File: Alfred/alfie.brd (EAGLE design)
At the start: 82.6 x 45 mm, 19 parts, among them IC1 7805TV, K1 G6A-234P, K2 G6A-234P

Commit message: Added diodes and resistors.
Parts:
- added D5, D6: 1N4148DO35-7, diode:DO35-7
- added R1: (no value), rcl:0207/10
- moved U$5 5.75 mm to (45.7, 10.2), turned to 90 degrees
- moved U$2 5.12 mm to (45.7, 21.6), turned to 90 degrees
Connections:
- net +5V: now also D5.C, D6.C
- net DOORBELL: now also R1.2
- net GND: now also R1.1
- net N$1: now also D6.A
- net N$2: now also D5.A
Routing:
- net +5V: track 166.1 -> 171.2 mm
- net N$2: track 5.60 -> 6.36 mm
- net N$1: track 5.86 -> 6.36 mm
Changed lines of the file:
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@@
 <element name="IC1" library="linear" package="TO220V" value="7805TV" x="53.34" y="38.1" rot="R90"/>
 <element name="C2" library="rcl" package="C025-030X050" value="" x="52.07" y="39.37" rot="R270"/>
-<element name="U$2" library="NTF3055L108" package="SOT223" value="NTF3055L108T1GTAB" x="46.355" y="26.67" rot="MR180"/>
+<element name="U$2" library="NTF3055L108" package="SOT223" value="NTF3055L108T1GTAB" x="45.72" y="21.59" rot="MR90"/>
 <element name="K1" library="relay" package="G6A-234P" value="G6A-234P" x="55.245" y="21.59">
 <attribute name="OC_NEWARK" value="unknown" x="55.245" y="21.59" size="1.778" layer="27" display="off"/>
@@
 <attribute name="OC_FARNELL" value="unknown" x="20.955" y="25.4" size="1.778" layer="27" rot="R270" display="off"/>
 </element>
-<element name="U$5" library="NTF3055L108" package="SOT223" value="NTF3055L108T1GTAB" x="46.355" y="15.875" rot="MR180"/>
+<element name="U$5" library="NTF3055L108" package="SOT223" value="NTF3055L108T1GTAB" x="45.72" y="10.16" rot="MR90"/>
 <element name="K2" library="relay" package="G6A-234P" value="G6A-234P" x="55.245" y="10.16">
 <attribute name="OC_NEWARK" value="unknown" x="46.355" y="10.16" size="1.778" layer="27" display="off"/>
@@
 <attribute name="OC_FARNELL" value="unknown" x="75.565" y="8.89" size="1.778" layer="27" rot="R90" display="off"/>
 </element>
+<element name="D5" library="diode" package="DO35-7" value="1N4148DO35-7" x="48.895" y="10.16" rot="R90"/>
+<element name="D6" library="diode" package="DO35-7" value="1N4148DO35-7" x="48.895" y="21.59" rot="R90"/>
+<element name="R1" library="rcl" package="0207/10" value="" x="39.37" y="35.56" rot="R90"/>
 </elements>
 <signals>
@@
 <wire x1="52.705" y1="17.78" x2="51.435" y2="17.78" width="0.8128" layer="16"/>
 <wire x1="51.435" y1="6.35" x2="53.975" y2="6.35" width="0.8128" layer="16"/>
+<contactref element="D5" pad="C"/>
+<contactref element="D6" pad="C"/>
+<wire x1="48.895" y1="6.35" x2="51.435" y2="6.35" width="0.8128" layer="16"/>
+<wire x1="48.895" y1="17.78" x2="51.435" y2="17.78" width="0.8128" layer="16"/>
 </signal>
 <signal name="GND">
@@
 <wire x1="11.035" y1="3.835" x2="10.4" y2="3.2" width="0.8128" layer="16"/>
 <wire x1="10.4" y1="3.2" x2="6.365" y2="3.2" width="0.8128" layer="16"/>
+<contactref element="R1" pad="1"/>
 </signal>
 <signal name="DATA0">
@@
 <wire x1="38.735" y1="35.56" x2="38.1" y2="34.925" width="0.8128" layer="16"/>
 <wire x1="38.1" y1="34.925" x2="36.83" y2="34.925" width="0.8128" layer="16"/>
+<contactref element="R1" pad="2"/>
 </signal>
 <signal name="N$1">
 <contactref element="K1" pad="16"/>
 <contactref element="U$2" pad="4"/>
-<wire x1="46.355" y1="23.52" x2="49.555" y2="23.52" width="0.8128" layer="16"/>
-<wire x1="49.555" y1="23.52" x2="51.435" y2="25.4" width="0.8128" layer="16"/>
+<contactref element="D6" pad="A"/>
+<wire x1="48.895" y1="25.4" x2="51.435" y2="25.4" width="0.8128" layer="16"/>
+<wire x1="48.895" y1="25.4" x2="48.895" y2="21.615" width="0.8128" layer="16"/>
+<wire x1="48.895" y1="21.615" x2="48.87" y2="21.59" width="0.8128" layer="16"/>
 </signal>
 <signal name="OUTER_DOOR_UNLOCK">
@@
 <contactref element="K2" pad="16"/>
 <contactref element="U$5" pad="4"/>
-<wire x1="46.355" y1="12.725" x2="50.19" y2="12.725" width="0.8128" layer="16"/>
-<wire x1="50.19" y1="12.725" x2="51.435" y2="13.97" width="0.8128" layer="16"/>
+<contactref element="D5" pad="A"/>
+<wire x1="48.895" y1="13.97" x2="51.435" y2="13.97" width="0.8128" layer="16"/>
+<wire x1="48.895" y1="13.97" x2="48.895" y2="10.185" width="0.8128" layer="16"/>
+<wire x1="48.895" y1="10.185" x2="48.87" y2="10.16" width="0.8128" layer="16"/>
 </signal>
 <signal name="INNER_DOOR_UNLOCK">

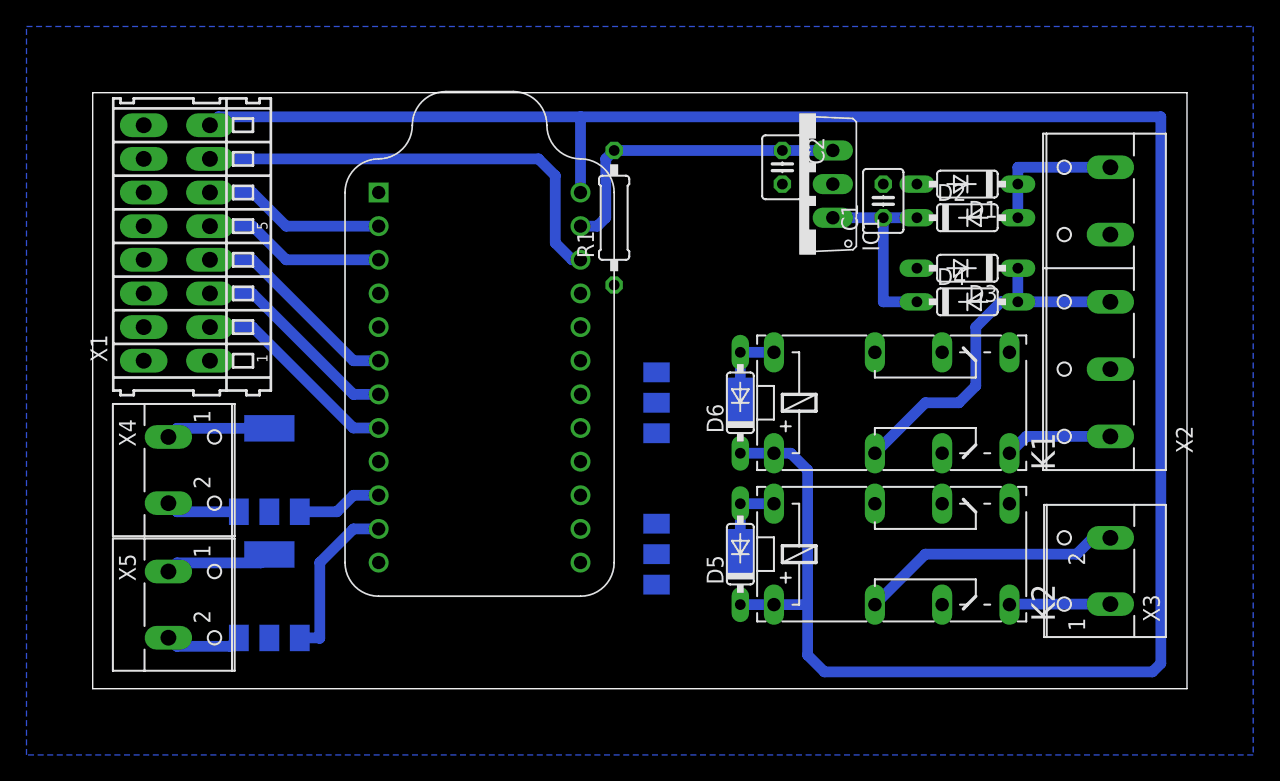
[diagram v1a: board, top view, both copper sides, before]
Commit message: Added expansion header, re routed the FETs a little
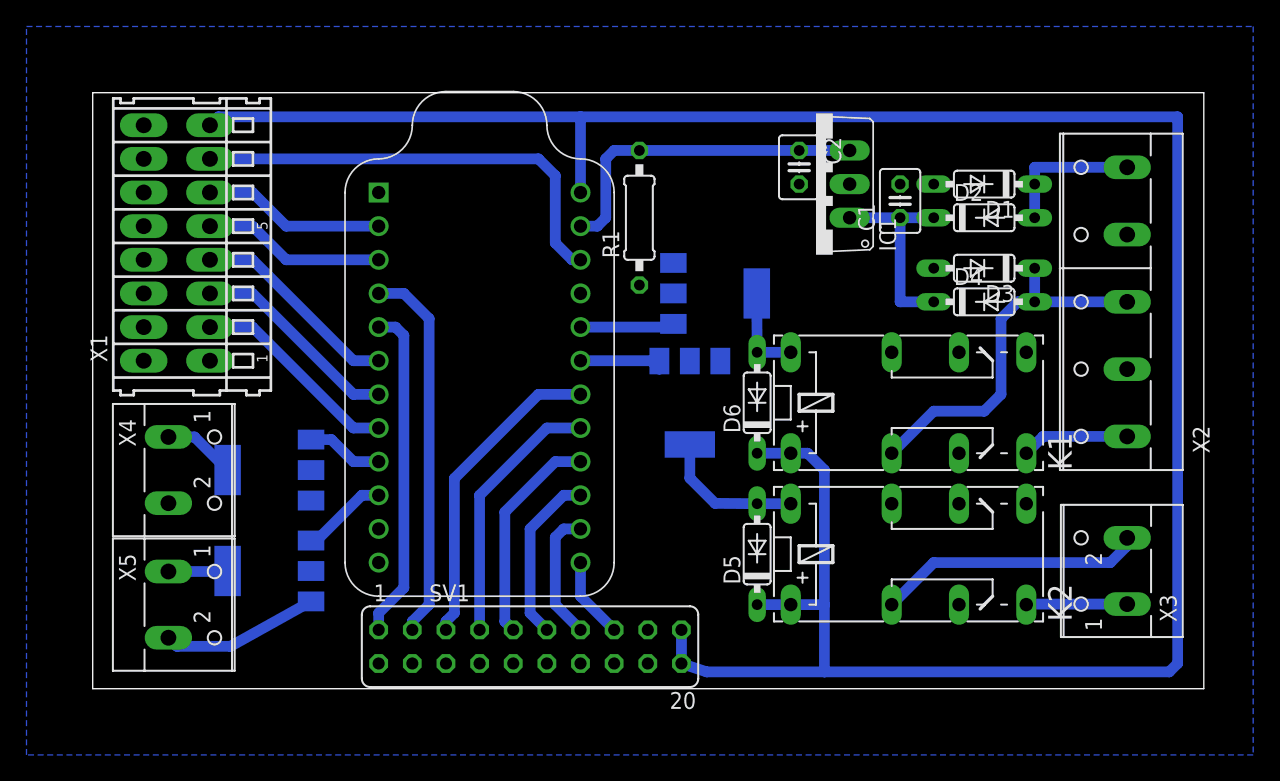
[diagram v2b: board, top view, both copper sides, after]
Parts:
- added SV1: (no value), con-lsta:FE10-2
- moved U$5 11.4 mm to (45.1, 21.6), turned to 180 degrees
- moved U$2 8.35 mm to (47.0, 29.8)
- moved R1 1.91 mm to (41.3, 35.6)
- moved U$4 1.91 mm to (13.3, 8.89), turned to 270 degrees
- moved C1 1.27 mm to (61.0, 36.8)
- moved C2 1.27 mm to (53.3, 39.4)
- moved K1 1.27 mm to (56.5, 21.6)
- moved K2 1.27 mm to (56.5, 10.2)
- moved D1 1.27 mm to (67.3, 38.1)
- moved D2 1.27 mm to (67.3, 35.6)
- moved D3 1.27 mm to (67.3, 31.8)
- moved D4 1.27 mm to (67.3, 29.2)
- moved D5 1.27 mm to (50.2, 10.2)
- moved D6 1.27 mm to (50.2, 21.6)
- moved IC1 1.27 mm to (54.6, 38.1)
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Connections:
- new net IO_1: SV1.5, U$1.PB7
- new net IO_2: SV1.7, U$1.PB6
- new net IO_3: SV1.9, U$1.PB5
- new net IO_4: SV1.11, U$1.PB4
- new net IO_5: SV1.13, U$1.PB3
- new net IO_6: SV1.15, U$1.PB2
- new net RX: SV1.3, U$1.PD2
- new net TX: SV1.1, U$1.PD3
- net +5V: now also SV1.19, SV1.20
- net GND: now also SV1.10, SV1.12, SV1.14, SV1.16, SV1.17, SV1.18, SV1.2, SV1.4, SV1.6, SV1.8
- net HC_OUT_1: now also U$1.PD7; no longer U$1.PB0
- net HC_OUT_2: now also U$1.PB0; no longer U$1.PB1
- net INNER_DOOR_UNLOCK: now also U$1.PC7
- net OUTER_DOOR_UNLOCK: now also U$1.PC6
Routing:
- net RX: track 0.00 -> 28.6 mm
- net TX: track 0.00 -> 25.2 mm
- net IO_1: track 0.00 -> 23.8 mm
- net IO_2: track 0.00 -> 19.9 mm
- net IO_3: track 0.00 -> 16.4 mm
- net +5V: track 171.2 -> 186.6 mm
- net IO_4: track 0.00 -> 13.0 mm
- net IO_5: track 0.00 -> 9.94 mm
- net OUTER_DOOR_UNLOCK: track 0.00 -> 7.11 mm
- net INNER_DOOR_UNLOCK: track 0.00 -> 6.83 mm
- net HC_OUT_2: track 12.7 -> 6.52 mm
- net IO_6: track 0.00 -> 6.13 mm
- net N$2: track 6.36 -> 10.9 mm
- net N$8: track 8.15 -> 4.49 mm
- net N$5: track 7.89 -> 5.51 mm
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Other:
- board size 82.6 x 45 mm -> 83.9 x 45 mm

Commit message: Added decoupling, tidied up schematic
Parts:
- added C10, C11, C12, C9: 100nF, rcl:C0805
- added C3, C4, C5, C6, C7, C8: 1nF, rcl:C0805
- moved X1 3.86 mm to (10.2, 34.3)
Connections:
- net +5V: now also C10.1, C11.1, C12.1, C9.1
- net BUZZER: now also C8.1
- net DATA0: now also C7.1
- net DATA1: now also C6.1
- net GND: now also C10.2, C11.2, C12.2, C3.2, C4.2, C5.2, C6.2, C7.2, C8.2, C9.2
- net LED_GREEN: now also C4.1
- net LED_RED: now also C3.1
- net SPARE_INPUT: now also C5.1
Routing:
- net +5V: track 186.6 -> 194.6 mm
- net SPARE_INPUT: track 15.9 -> 23.4 mm
- net LED_RED: track 15.9 -> 23.4 mm
- net LED_GREEN: track 15.9 -> 23.4 mm
- net DATA1: track 13.8 -> 19.4 mm
- net BUZZER: track 34.1 -> 39.7 mm
- net DATA0: track 13.8 -> 19.4 mm
